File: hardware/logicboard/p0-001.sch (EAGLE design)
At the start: 24 parts, among them IC1 74ALS05N, IC2 LTC485N, IC3 LTC485N, J0 DC5V, J1 DIN5, J2 DIN5, J3 DIN5, X1 NELTRON-7810-XPXC, X2 NELTRON-7810-XPXC

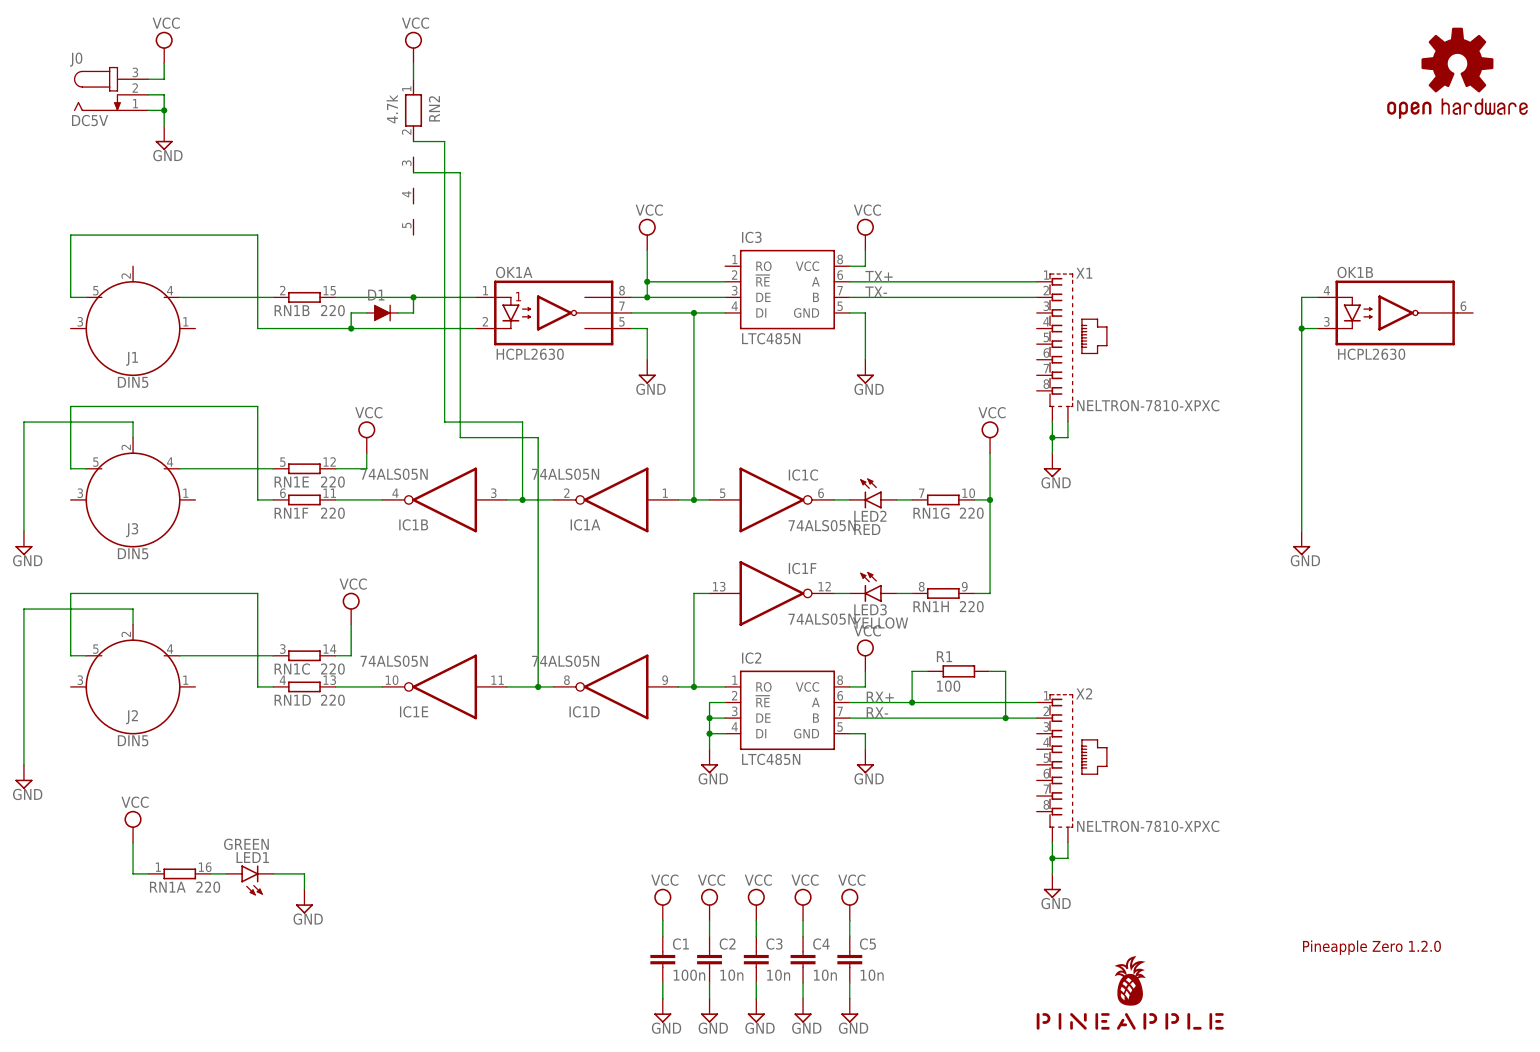
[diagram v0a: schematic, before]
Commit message: Fixed pull-up.
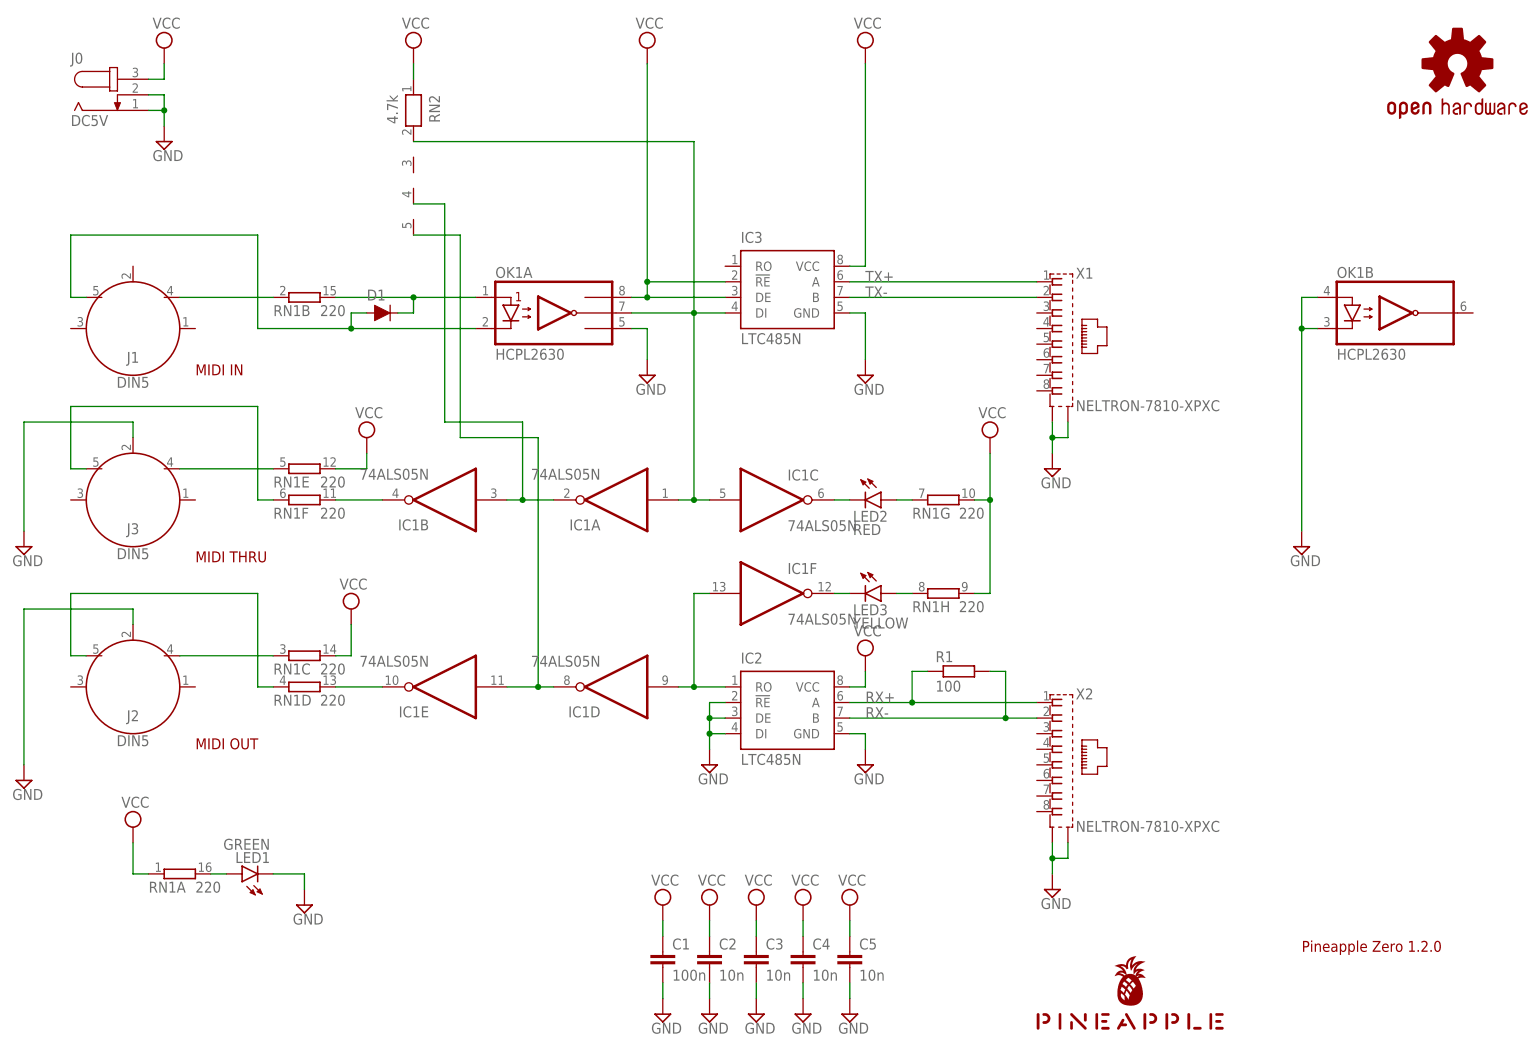
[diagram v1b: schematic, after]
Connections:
- net NMIDIOUT: now also RN2.5; no longer RN2.3
- net NMIDITHRU: now also RN2.4; no longer RN2.2
- net TX: now also RN2.2
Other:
- note added: "MIDI IN"
- note added: "MIDI OUT"
- note added: "MIDI THRU"
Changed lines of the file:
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@@
 <plain>
 <text x="215.9" y="20.32" size="1.778" layer="94">Pineapple Zero 1.2.0</text>
+<text x="35.56" y="114.3" size="1.778" layer="94">MIDI IN</text>
+<text x="35.56" y="83.82" size="1.778" layer="94">MIDI THRU</text>
+<text x="35.56" y="53.34" size="1.778" layer="94">MIDI OUT</text>
 </plain>
 <instances>
@@
 <attribute name="VALUE" x="117.475" y="47.625" size="1.778" layer="96"/>
 </instance>
-<instance part="SUPPLY4" gate="G$1" x="109.22" y="137.16" smashed="yes">
-<attribute name="VALUE" x="107.315" y="140.335" size="1.778" layer="96"/>
+<instance part="SUPPLY4" gate="G$1" x="109.22" y="167.64" smashed="yes">
+<attribute name="VALUE" x="107.315" y="170.815" size="1.778" layer="96"/>
 </instance>
 <instance part="SUPPLY14" gate="GND" x="144.78" y="114.3" smashed="yes">
@@
 <attribute name="VALUE" x="28.575" y="170.815" size="1.778" layer="96"/>
 </instance>
-<instance part="SUPPLY13" gate="G$1" x="144.78" y="137.16" smashed="yes">
-<attribute name="VALUE" x="142.875" y="140.335" size="1.778" layer="96"/>
+<instance part="SUPPLY13" gate="G$1" x="144.78" y="167.64" smashed="yes">
+<attribute name="VALUE" x="142.875" y="170.815" size="1.778" layer="96"/>
 </instance>
 <instance part="SUPPLY2" gate="G$1" x="60.96" y="76.2" smashed="yes">
@@
 <segment>
 <pinref part="SUPPLY13" gate="G$1" pin="VCC"/>
-<wire x1="144.78" y1="132.08" x2="144.78" y2="134.62" width="0.1524" layer="91"/>
+<wire x1="144.78" y1="132.08" x2="144.78" y2="165.1" width="0.1524" layer="91"/>
 <pinref part="IC3" gate="G$1" pin="VCC"/>
 <wire x1="142.24" y1="132.08" x2="144.78" y2="132.08" width="0.1524" layer="91"/>
@@
 <segment>
 <pinref part="SUPPLY4" gate="G$1" pin="VCC"/>
-<wire x1="109.22" y1="134.62" x2="109.22" y2="129.54" width="0.1524" layer="91"/>
+<wire x1="109.22" y1="165.1" x2="109.22" y2="129.54" width="0.1524" layer="91"/>
 <pinref part="OK1" gate="A" pin="VCC"/>
 <wire x1="109.22" y1="129.54" x2="109.22" y2="127" width="0.1524" layer="91"/>
@@
 <wire x1="119.38" y1="93.98" x2="116.84" y2="93.98" width="0.1524" layer="91"/>
 <junction x="116.84" y="93.98"/>
+<pinref part="RN2" gate="1" pin="2"/>
+<wire x1="71.12" y1="152.4" x2="116.84" y2="152.4" width="0.1524" layer="91"/>
+<wire x1="116.84" y1="152.4" x2="116.84" y2="124.46" width="0.1524" layer="91"/>
 </segment>
 </net>
@@
 <pinref part="IC1" gate="B" pin="I"/>
 <wire x1="93.98" y1="93.98" x2="88.9" y2="93.98" width="0.1524" layer="91"/>
-<pinref part="RN2" gate="1" pin="2"/>
 <wire x1="88.9" y1="93.98" x2="86.36" y2="93.98" width="0.1524" layer="91"/>
-<wire x1="71.12" y1="152.4" x2="76.2" y2="152.4" width="0.1524" layer="91"/>
-<wire x1="76.2" y1="152.4" x2="76.2" y2="106.68" width="0.1524" layer="91"/>
 <wire x1="76.2" y1="106.68" x2="88.9" y2="106.68" width="0.1524" layer="91"/>
 <wire x1="88.9" y1="106.68" x2="88.9" y2="93.98" width="0.1524" layer="91"/>
 <junction x="88.9" y="93.98"/>
+<pinref part="RN2" gate="1" pin="4"/>
+<wire x1="71.12" y1="142.24" x2="76.2" y2="142.24" width="0.1524" layer="91"/>
+<wire x1="76.2" y1="142.24" x2="76.2" y2="106.68" width="0.1524" layer="91"/>
 </segment>
 </net>
@@
 <pinref part="IC1" gate="E" pin="I"/>
 <wire x1="93.98" y1="63.5" x2="91.44" y2="63.5" width="0.1524" layer="91"/>
-<pinref part="RN2" gate="1" pin="3"/>
 <wire x1="91.44" y1="63.5" x2="86.36" y2="63.5" width="0.1524" layer="91"/>
-<wire x1="71.12" y1="147.32" x2="78.74" y2="147.32" width="0.1524" layer="91"/>
-<wire x1="78.74" y1="147.32" x2="78.74" y2="104.14" width="0.1524" layer="91"/>
 <wire x1="78.74" y1="104.14" x2="91.44" y2="104.14" width="0.1524" layer="91"/>
 <wire x1="91.44" y1="104.14" x2="91.44" y2="63.5" width="0.1524" layer="91"/>
 <junction x="91.44" y="63.5"/>
-</segment>
-</net>
+<pinref part="RN2" gate="1" pin="5"/>
+<wire x1="71.12" y1="137.16" x2="78.74" y2="137.16" width="0.1524" layer="91"/>
+<wire x1="78.74" y1="137.16" x2="78.74" y2="104.14" width="0.1524" layer="91"/>
+</segment>
+</net>

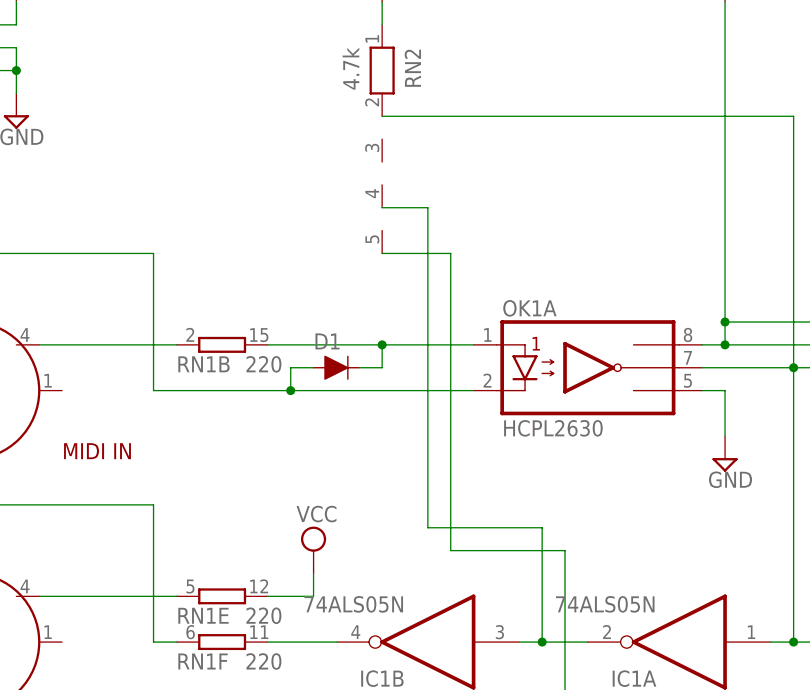
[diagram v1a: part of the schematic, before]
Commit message: Swapped MIDI IN and THRU, TX and RX.
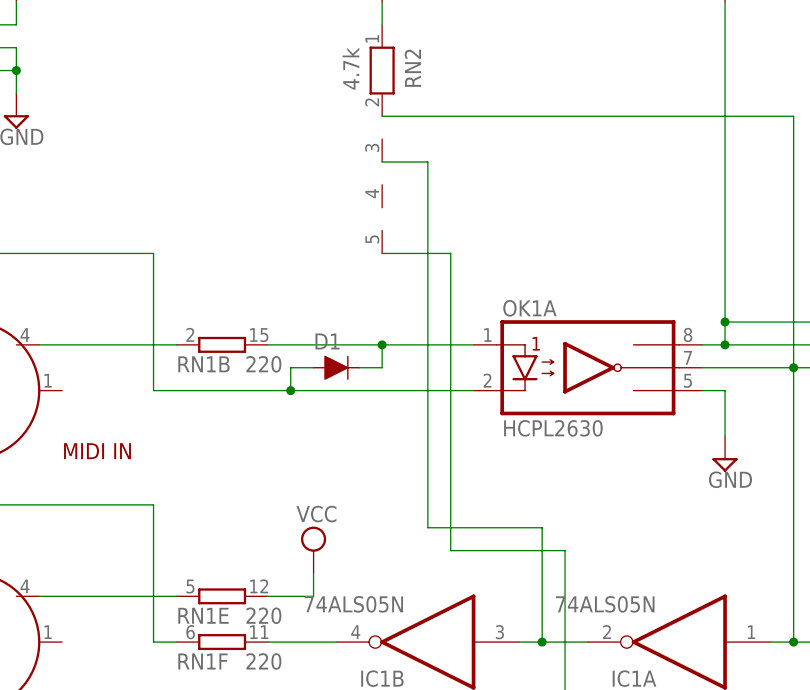
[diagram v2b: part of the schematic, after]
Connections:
- net NMIDITHRU: now also RN2.3; no longer RN2.4
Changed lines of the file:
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@@
 <wire x1="88.9" y1="106.68" x2="88.9" y2="93.98" width="0.1524" layer="91"/>
 <junction x="88.9" y="93.98"/>
-<pinref part="RN2" gate="1" pin="4"/>
-<wire x1="71.12" y1="142.24" x2="76.2" y2="142.24" width="0.1524" layer="91"/>
-<wire x1="76.2" y1="142.24" x2="76.2" y2="106.68" width="0.1524" layer="91"/>
+<wire x1="76.2" y1="147.32" x2="76.2" y2="106.68" width="0.1524" layer="91"/>
+<pinref part="RN2" gate="1" pin="3"/>
+<wire x1="71.12" y1="147.32" x2="76.2" y2="147.32" width="0.1524" layer="91"/>
 </segment>
 </net>
